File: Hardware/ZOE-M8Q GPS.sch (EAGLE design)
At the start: 31 parts, among them J4 U.FL, U1 UBLOX_ZOE_M8-0-10, Y1 32.768kHz

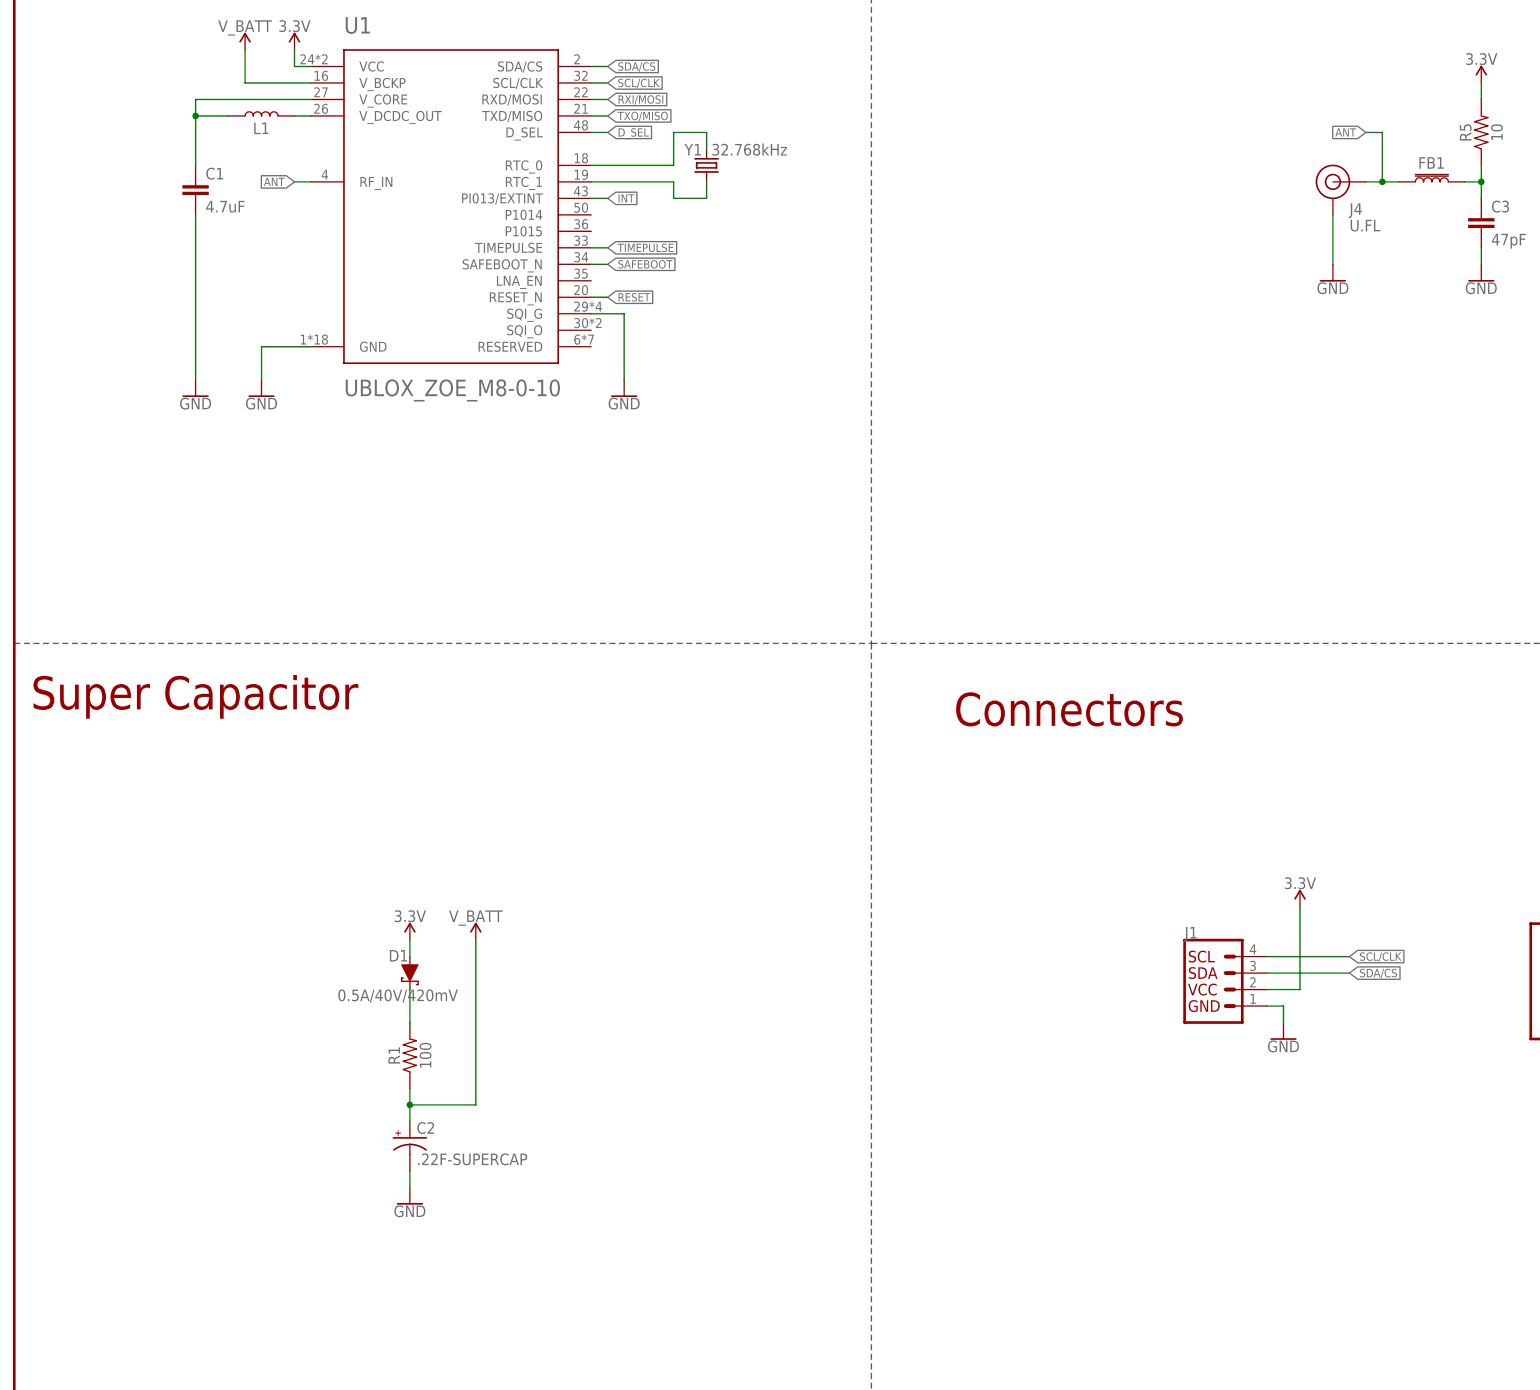
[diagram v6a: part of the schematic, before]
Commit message: Adds new reflowable battery, updates battery, inductor, and IC with versions in the SparkFun Eagle Library
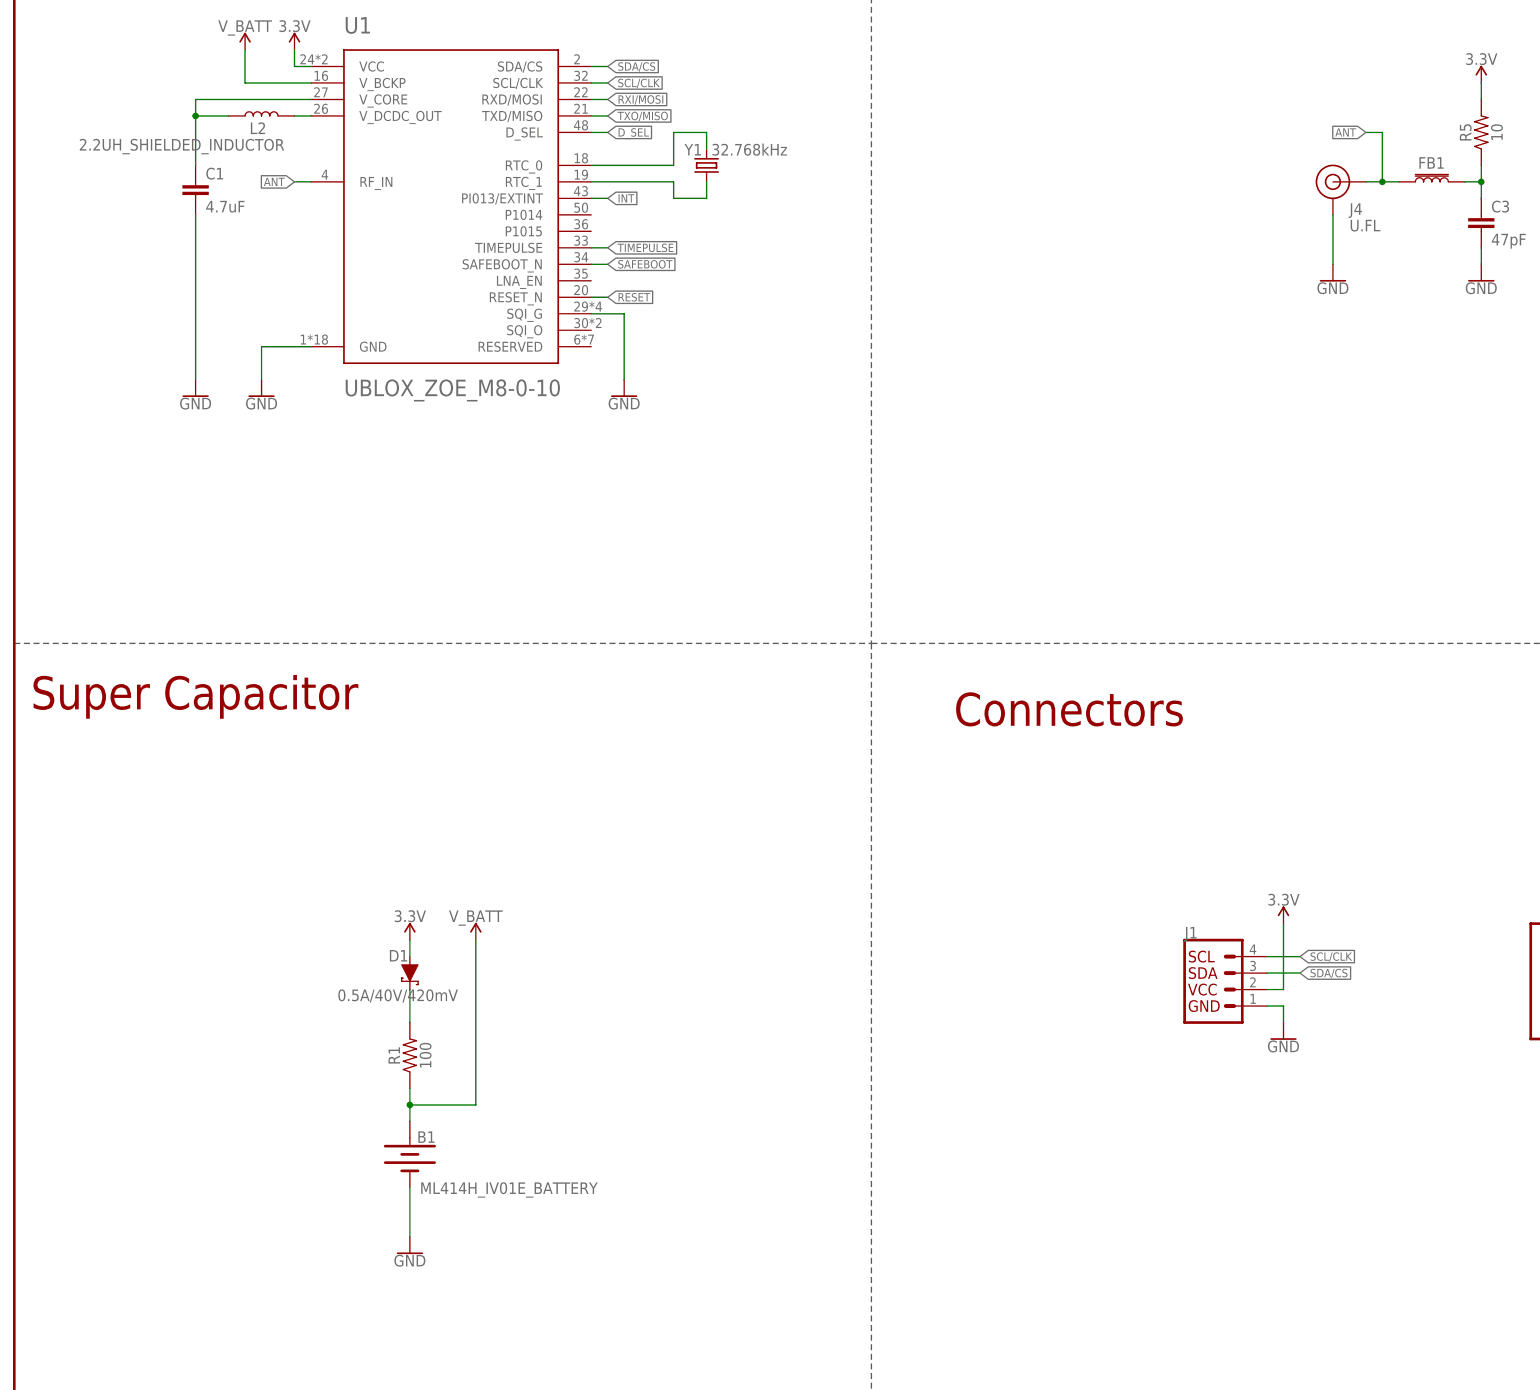
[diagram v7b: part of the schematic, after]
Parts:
- removed C2: .22F-SUPERCAP, SparkFun-Capacitors:.22F-SUPERCAP
- removed L1: 2.2UH_SHIELDED_INDUCTOR, temp:2.2UH_SHIELDED_INDUCTOR
- added B1: ML414H_IV01E_BATTERY, SparkFun-Batteries:ML414H_IV01E_BATTERY
- added L2: 2.2UH_SHIELDED_INDUCTOR, SparkFun-Coils:2.2UH_SHIELDED_INDUCTOR
- U1: device temp:UBLOX_ZOE_M8-0-10 -> SparkFun-GPS:UBLOX_ZOE_M8-0-10
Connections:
- net GND: now also B1.-; no longer C2.-
- net N$6: now also L2.1; no longer L1.1
- net N$7: now also L2.2; no longer L1.2
- net V_BATT: now also B1.+; no longer C2.+
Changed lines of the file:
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@@
 <parts>
 <part name="FRAME1" library="SparkFun-Aesthetics" deviceset="FRAME-LEDGER" device=""/>
-<part name="U1" library="temp" deviceset="UBLOX_ZOE_M8-0-10" device=""/>
+<part name="U1" library="SparkFun-GPS" deviceset="UBLOX_ZOE_M8-0-10" device=""/>
 <part name="J1" library="SparkFun-Connectors" deviceset="QWIIC_CONNECTOR" device="JS-1MM"/>
 <part name="R3" library="SparkFun-Resistors" deviceset="2.2KOHM" device="-0603-1/10W-1%" value="2.2k"/>
@@
 <part name="GND5" library="SparkFun-PowerSymbols" deviceset="GND" device=""/>
 <part name="JP4" library="SparkFun-Jumpers" deviceset="JUMPER-SMT_2_NC_TRACE" device="_SILK" value="JUMPER-SMT_2_NC_TRACE_SILK"/>
-<part name="C2" library="SparkFun-Capacitors" deviceset=".22F-SUPERCAP" device=""/>
 <part name="FB1" library="SparkFun-Coils" deviceset="FERRITE_BEAD-120_OHM" device="-0402"/>
 <part name="R5" library="SparkFun-Resistors" deviceset="10OHM" device="-0603-1/10W-1%" value="10"/>
@@
 <part name="GND7" library="SparkFun-PowerSymbols" deviceset="GND" device=""/>
 <part name="SUPPLY9" library="SparkFun-PowerSymbols" deviceset="3.3V" device=""/>
-<part name="L1" library="temp" deviceset="2.2UH_SHIELDED_INDUCTOR" device=""/>
+<part name="B1" library="SparkFun-Batteries" deviceset="ML414H_IV01E_BATTERY" device=""/>
+<part name="L2" library="SparkFun-Coils" deviceset="2.2UH_SHIELDED_INDUCTOR" device=""/>
 </parts>
 <sheets>
@@
 <attribute name="VALUE" x="93.98" y="167.386" size="1.778" layer="96" align="top-center"/>
 </instance>
-<instance part="GND10" gate="1" x="60.96" y="43.18" smashed="yes">
-<attribute name="VALUE" x="60.96" y="42.926" size="1.778" layer="96" align="top-center"/>
-</instance>
-<instance part="SUPPLY8" gate="G$1" x="198.12" y="88.9" smashed="yes">
-<attribute name="VALUE" x="198.12" y="91.694" size="1.778" layer="96" align="bottom-center"/>
+<instance part="GND10" gate="1" x="60.96" y="35.56" smashed="yes">
+<attribute name="VALUE" x="60.96" y="35.306" size="1.778" layer="96" align="top-center"/>
+</instance>
+<instance part="SUPPLY8" gate="G$1" x="195.58" y="86.36" smashed="yes">
+<attribute name="VALUE" x="195.58" y="89.154" size="1.778" layer="96" align="bottom-center"/>
 </instance>
 <instance part="J3" gate="G$1" x="238.76" y="76.2" smashed="yes">
@@
 <attribute name="NAME" x="335.28" y="182.88" size="1.778" layer="95" font="vector" rot="R180"/>
 </instance>
-<instance part="C2" gate="G$1" x="60.96" y="53.34" smashed="yes">
-<attribute name="NAME" x="61.976" y="53.975" size="1.778" layer="95" font="vector"/>
-<attribute name="VALUE" x="61.976" y="49.149" size="1.778" layer="96" font="vector"/>
-</instance>
 <instance part="FB1" gate="G$1" x="218.44" y="200.66" smashed="yes" rot="R90">
 <attribute name="NAME" x="220.472" y="204.47" size="1.778" layer="95" font="vector" rot="R180"/>
@@
 <attribute name="VALUE" x="226.06" y="218.694" size="1.778" layer="96" align="bottom-center"/>
 </instance>
-<instance part="L1" gate="G$1" x="38.1" y="210.82" smashed="yes" rot="R90">
-<attribute name="NAME" x="39.37" y="209.804" size="1.778" layer="95" font="vector" rot="R180"/>
+<instance part="B1" gate="G$1" x="60.96" y="50.8" smashed="yes" rot="R270">
+<attribute name="NAME" x="63.5" y="52.578" size="1.778" layer="95" font="vector" align="bottom-center"/>
+<attribute name="VALUE" x="76.2" y="46.482" size="1.778" layer="96" font="vector" align="top-center"/>
+</instance>
+<instance part="L2" gate="G$1" x="38.1" y="210.82" smashed="yes" rot="R90">
+<attribute name="NAME" x="38.862" y="209.804" size="1.778" layer="95" font="vector" rot="R180"/>
+<attribute name="VALUE" x="41.656" y="205.486" size="1.778" layer="96" font="vector" rot="R180" align="top-left"/>
 </instance>
 </instances>
@@
 <segment>
 <pinref part="GND10" gate="1" pin="GND"/>
-<wire x1="60.96" y1="45.72" x2="60.96" y2="48.26" width="0.1524" layer="91"/>
-<pinref part="C2" gate="G$1" pin="-"/>
+<wire x1="60.96" y1="38.1" x2="60.96" y2="45.72" width="0.1524" layer="91"/>
+<pinref part="B1" gate="G$1" pin="-"/>
 </segment>
 <segment>
@@
 <segment>
 <pinref part="J1" gate="G$1" pin="2"/>
-<wire x1="198.12" y1="76.2" x2="198.12" y2="88.9" width="0.1524" layer="91"/>
-<wire x1="193.04" y1="76.2" x2="198.12" y2="76.2" width="0.1524" layer="91"/>
+<wire x1="195.58" y1="76.2" x2="195.58" y2="86.36" width="0.1524" layer="91"/>
+<wire x1="193.04" y1="76.2" x2="195.58" y2="76.2" width="0.1524" layer="91"/>
 <pinref part="SUPPLY8" gate="G$1" pin="3.3V"/>
 </segment>
@@
 <segment>
 <pinref part="J1" gate="G$1" pin="3"/>
-<wire x1="193.04" y1="78.74" x2="205.74" y2="78.74" width="0.1524" layer="91"/>
-<label x="205.74" y="78.74" size="1.27" layer="95" xref="yes"/>
+<wire x1="193.04" y1="78.74" x2="198.12" y2="78.74" width="0.1524" layer="91"/>
+<label x="198.12" y="78.74" size="1.27" layer="95" xref="yes"/>
 </segment>
 <segment>
@@
 <segment>
 <pinref part="J1" gate="G$1" pin="4"/>
-<wire x1="205.74" y1="81.28" x2="193.04" y2="81.28" width="0.1524" layer="91"/>
-<label x="205.74" y="81.28" size="1.27" layer="95" xref="yes"/>
+<wire x1="198.12" y1="81.28" x2="193.04" y2="81.28" width="0.1524" layer="91"/>
+<label x="198.12" y="81.28" size="1.27" layer="95" xref="yes"/>
 </segment>
 <segment>
@@
 <pinref part="U1" gate="G$1" pin="V_DCDC_OUT"/>
 <wire x1="45.72" y1="210.82" x2="43.18" y2="210.82" width="0.1524" layer="91"/>
-<pinref part="L1" gate="G$1" pin="2"/>
+<pinref part="L2" gate="G$1" pin="2"/>
 </segment>
 </net>
@@
 <wire x1="27.94" y1="210.82" x2="27.94" y2="203.2" width="0.1524" layer="91"/>
 <junction x="27.94" y="210.82"/>
-<pinref part="L1" gate="G$1" pin="1"/>
+<pinref part="L2" gate="G$1" pin="1"/>
 </segment>
 </net>
@@
 <pinref part="SUPPLY1" gate="G$1" pin="V_BATT"/>
 <wire x1="71.12" y1="58.42" x2="71.12" y2="83.82" width="0.1524" layer="91"/>
-<pinref part="C2" gate="G$1" pin="+"/>
-</segment>
-</net>
+<pinref part="B1" gate="G$1" pin="+"/>
+</segment>
+</net>
